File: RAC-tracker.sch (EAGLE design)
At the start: 27 parts, among them J1 U.FL, J2 U.FL, U1 NRF9160-SICA-R, U2 SIM-ST-MFF2, U3 MCP73831, U4 SKY65723-81, U5 MIC5365-1.8YC5-TR

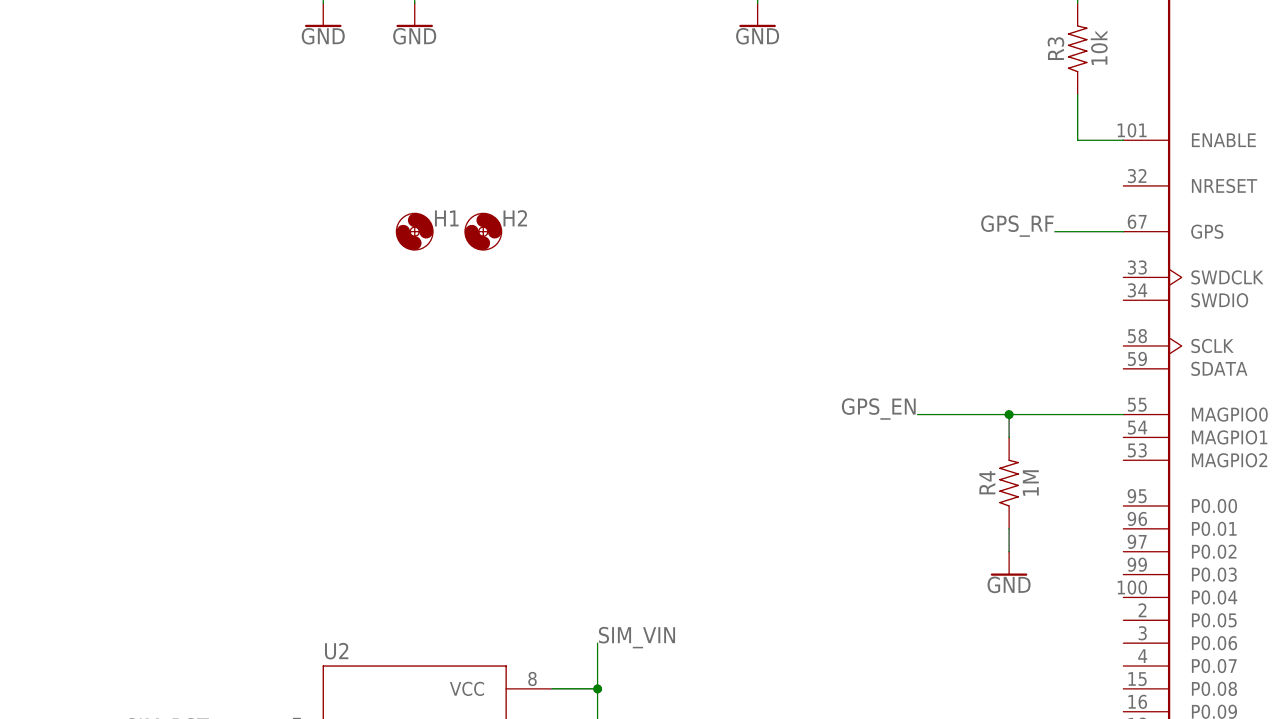
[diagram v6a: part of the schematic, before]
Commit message: Completed routing, cleared DRC errors
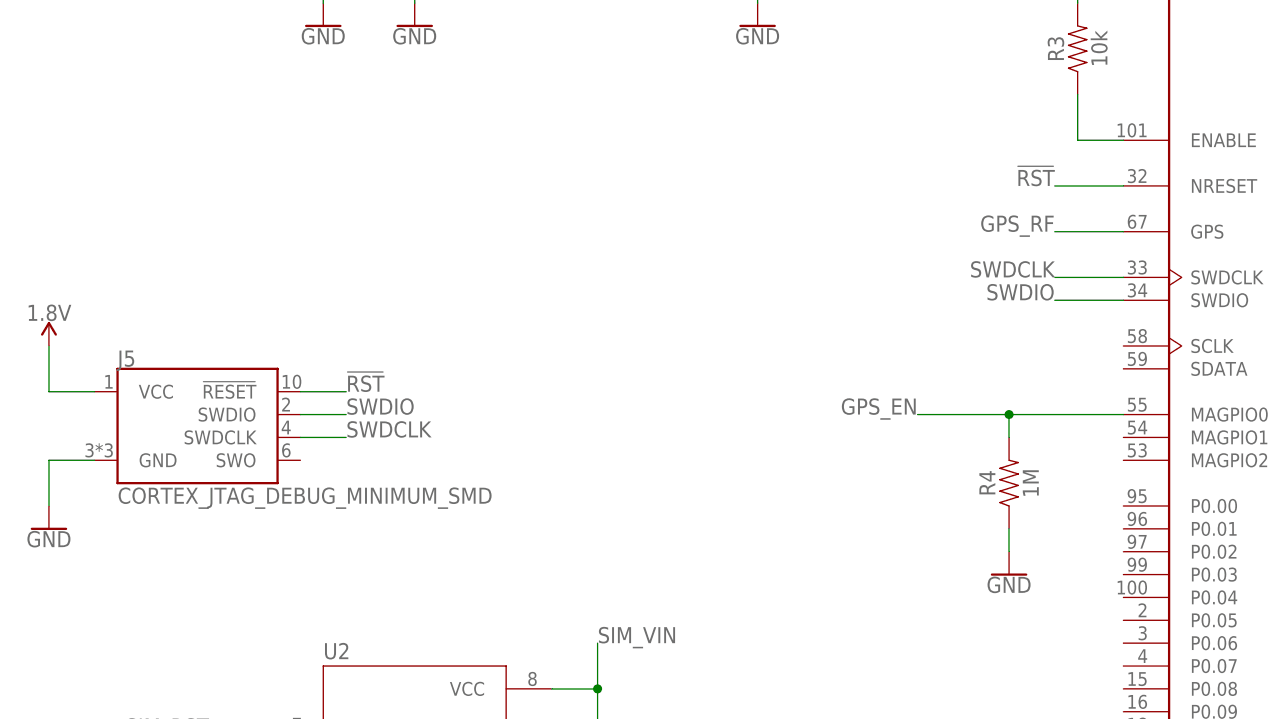
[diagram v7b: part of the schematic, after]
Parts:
- removed H1, H2: MOUNT-HOLE2.8, holes:MOUNT-HOLE2.8
- added J5: CORTEX_JTAG_DEBUG_MINIMUM_SMD, SparkFun-Connectors:CORTEX_JTAG_DEBUG_MINIMUM_SMD
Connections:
- new net !RST: J5.!RESET, U1.NRESET
- new net SWDCLK: J5.SWDCLK, U1.SWDCLK
- new net SWDIO: J5.SWDIO, U1.SWDIO
- net 1.8V: now also J5.VCC
- net GND: now also J5.GND
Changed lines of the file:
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@@
 </classes>
 <parts>
-<part name="H1" library="holes" library_urn="urn:adsk.eagle:library:237" deviceset="MOUNT-HOLE" device="2.8" package3d_urn="urn:adsk.eagle:package:14271/1"/>
-<part name="H2" library="holes" library_urn="urn:adsk.eagle:library:237" deviceset="MOUNT-HOLE" device="2.8" package3d_urn="urn:adsk.eagle:package:14271/1"/>
 <part name="U2" library="rocket-components" deviceset="SIM-ST-MFF2" device=""/>
 <part name="C5" library="SparkFun-Capacitors" library_urn="urn:adsk.eagle:library:510" deviceset="0.1UF" device="-0603-25V-(+80/-20%)" package3d_urn="urn:adsk.eagle:package:37414/1" value="0.1uF"/>
@@
 <part name="SUPPLY16" library="SparkFun-PowerSymbols" library_urn="urn:adsk.eagle:library:530" deviceset="1.8V" device=""/>
 <part name="GND18" library="SparkFun-PowerSymbols" library_urn="urn:adsk.eagle:library:530" deviceset="GND" device=""/>
+<part name="J5" library="SparkFun-Connectors" deviceset="CORTEX_JTAG_DEBUG_MINIMUM" device="_SMD"/>
+<part name="SUPPLY2" library="SparkFun-PowerSymbols" library_urn="urn:adsk.eagle:library:530" deviceset="1.8V" device=""/>
+<part name="GND19" library="SparkFun-PowerSymbols" library_urn="urn:adsk.eagle:library:530" deviceset="GND" device=""/>
 </parts>
 <sheets>
@@
 </plain>
 <instances>
-<instance part="H1" gate="G$1" x="-40.64" y="33.02" smashed="yes">
-<attribute name="NAME" x="-38.608" y="33.6042" size="1.778" layer="95"/>
-</instance>
-<instance part="H2" gate="G$1" x="-33.02" y="33.02" smashed="yes">
-<attribute name="NAME" x="-30.988" y="33.6042" size="1.778" layer="95"/>
-</instance>
 <instance part="U2" gate="G$1" x="-40.64" y="-27.94" smashed="yes">
 <attribute name="NAME" x="-50.8" y="-14.478" size="1.778" layer="95"/>
@@
 <instance part="GND18" gate="1" x="-40.64" y="55.88" smashed="yes">
 <attribute name="VALUE" x="-40.64" y="55.626" size="1.778" layer="96" align="top-center"/>
+</instance>
+<instance part="J5" gate="G$1" x="-63.5" y="10.16" smashed="yes">
+<attribute name="NAME" x="-73.66" y="18.034" size="1.778" layer="95" font="vector"/>
+<attribute name="VALUE" x="-73.66" y="2.794" size="1.778" layer="96" font="vector"/>
+</instance>
+<instance part="SUPPLY2" gate="G$1" x="-81.28" y="20.32" smashed="yes">
+<attribute name="VALUE" x="-81.28" y="23.114" size="1.778" layer="96" align="bottom-center"/>
+</instance>
+<instance part="GND19" gate="1" x="-81.28" y="0" smashed="yes">
+<attribute name="VALUE" x="-81.28" y="-0.254" size="1.778" layer="96" align="top-center"/>
 </instance>
 </instances>
@@
 <wire x1="-40.64" y1="73.66" x2="-35.56" y2="73.66" width="0.1524" layer="91"/>
 </segment>
+<segment>
+<pinref part="GND19" gate="1" pin="GND"/>
+<wire x1="-81.28" y1="2.54" x2="-81.28" y2="7.62" width="0.1524" layer="91"/>
+<pinref part="J5" gate="G$1" pin="GND"/>
+<wire x1="-81.28" y1="7.62" x2="-76.2" y2="7.62" width="0.1524" layer="91"/>
+</segment>
 </net>
 <net name="SIM_VIN" class="0">
@@
 <pinref part="SUPPLY16" gate="G$1" pin="1.8V"/>
 </segment>
-</net>
+<segment>
+<pinref part="J5" gate="G$1" pin="VCC"/>
+<wire x1="-76.2" y1="15.24" x2="-81.28" y2="15.24" width="0.1524" layer="91"/>
+<pinref part="SUPPLY2" gate="G$1" pin="1.8V"/>
+<wire x1="-81.28" y1="15.24" x2="-81.28" y2="20.32" width="0.1524" layer="91"/>
+</segment>
+</net>
+<net name="!RST" class="0">
+<segment>
+<pinref part="U1" gate="G$1" pin="NRESET"/>
+<wire x1="38.1" y1="38.1" x2="30.48" y2="38.1" width="0.1524" layer="91"/>
+<label x="30.48" y="38.1" size="1.778" layer="95" rot="MR0"/>
+</segment>
+<segment>
+<pinref part="J5" gate="G$1" pin="!RESET"/>
+<wire x1="-53.34" y1="15.24" x2="-48.26" y2="15.24" width="0.1524" layer="91"/>
+<label x="-48.26" y="15.24" size="1.778" layer="95"/>
+</segment>
+</net>
+<net name="SWDCLK" class="0">
+<segment>
+<pinref part="U1" gate="G$1" pin="SWDCLK"/>
+<wire x1="38.1" y1="27.94" x2="30.48" y2="27.94" width="0.1524" layer="91"/>
+<label x="30.48" y="27.94" size="1.778" layer="95" rot="MR0"/>
+</segment>
+<segment>
+<pinref part="J5" gate="G$1" pin="SWDCLK"/>
+<wire x1="-53.34" y1="10.16" x2="-48.26" y2="10.16" width="0.1524" layer="91"/>
+<label x="-48.26" y="10.16" size="1.778" layer="95"/>
+</segment>
+</net>
+<net name="SWDIO" class="0">
+<segment>
+<pinref part="U1" gate="G$1" pin="SWDIO"/>
+<wire x1="38.1" y1="25.4" x2="30.48" y2="25.4" width="0.1524" layer="91"/>
+<label x="30.48" y="25.4" size="1.778" layer="95" rot="MR0"/>
+</segment>
+<segment>
+<pinref part="J5" gate="G$1" pin="SWDIO"/>
+<wire x1="-53.34" y1="12.7" x2="-48.26" y2="12.7" width="0.1524" layer="91"/>
+<label x="-48.26" y="12.7" size="1.778" layer="95"/>
+</segment>
+</net>

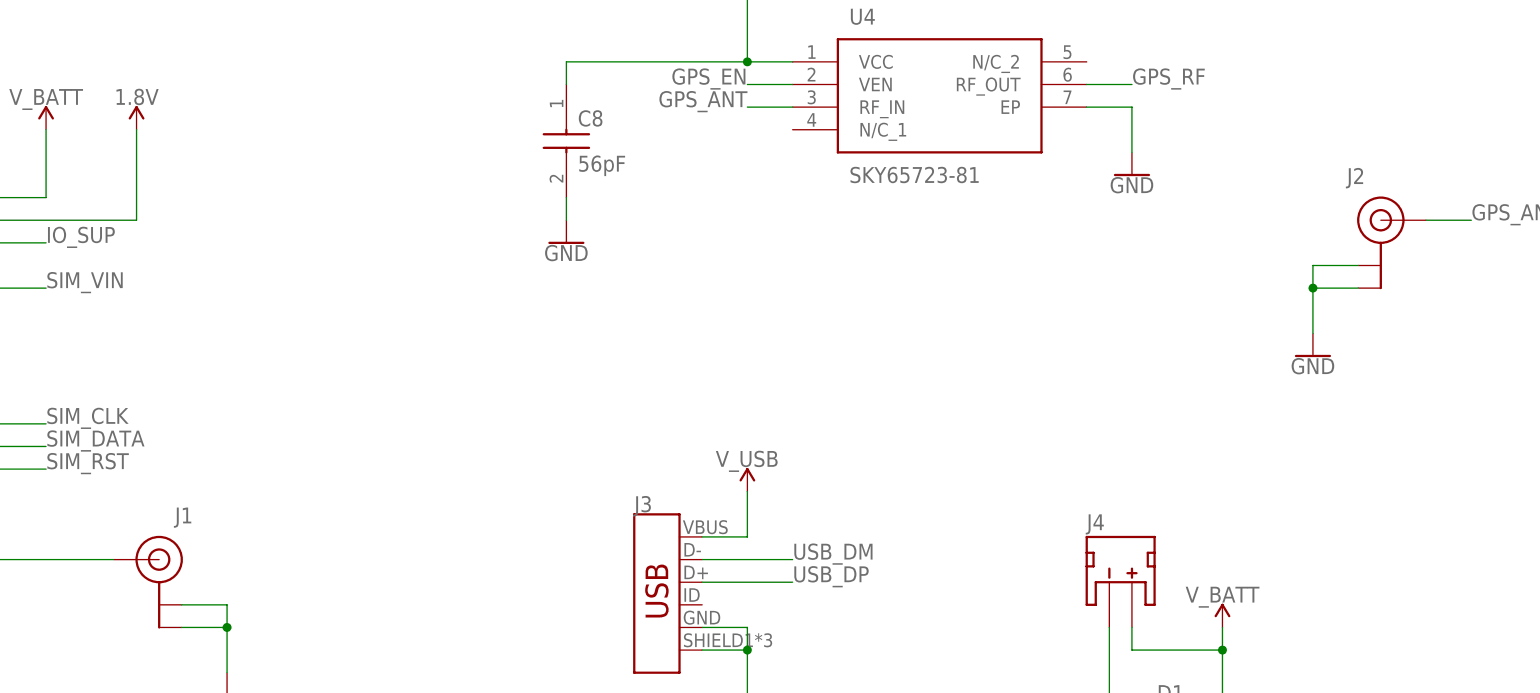
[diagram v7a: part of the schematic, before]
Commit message: Stitched vias in the top ground plane. Ready for fabrication!
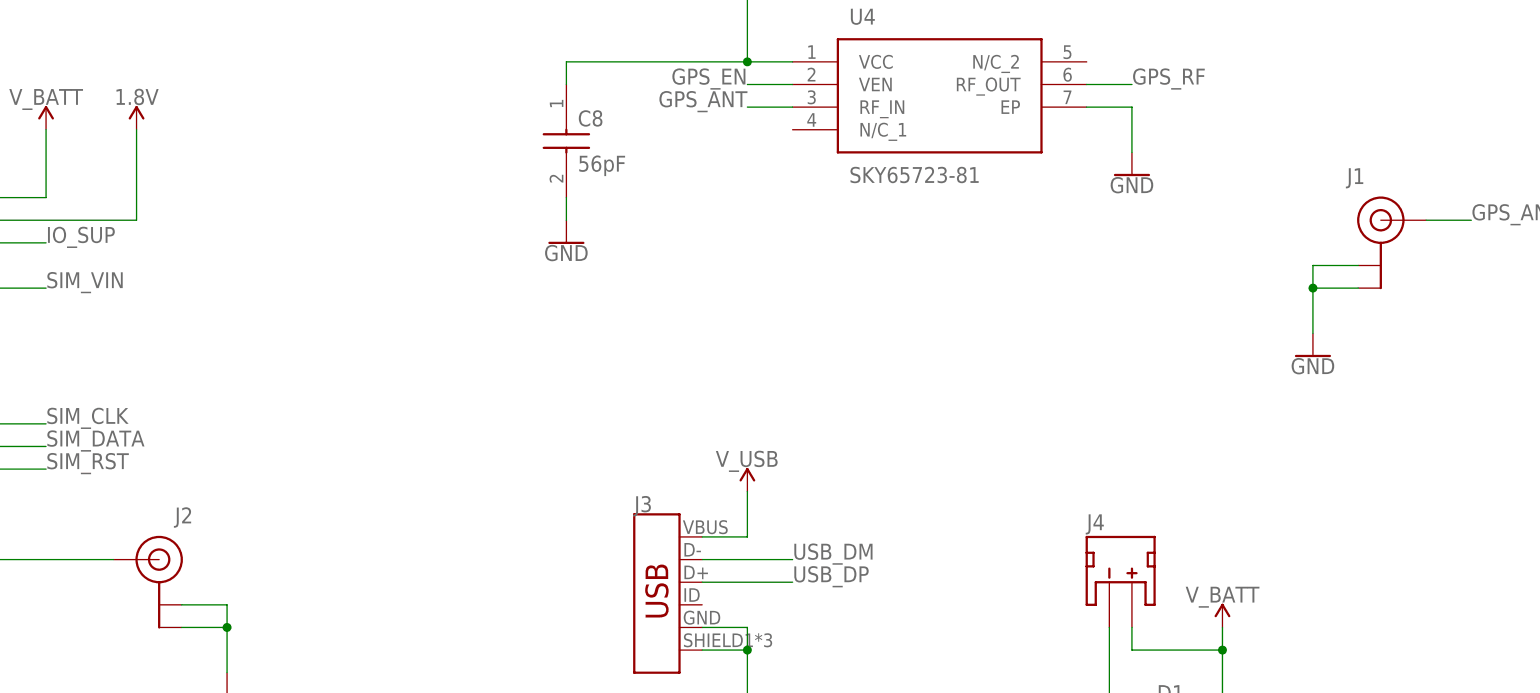
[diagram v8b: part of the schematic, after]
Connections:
- net GPS_ANT: now also J1.SIGNAL; no longer J2.SIGNAL
- net LTE_ANT: now also J2.SIGNAL; no longer J1.SIGNAL
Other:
- moved on the sheet: J1, J2
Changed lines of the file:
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@@
 <part name="R3" library="SparkFun-Resistors" library_urn="urn:adsk.eagle:library:532" deviceset="10KOHM" device="-0603-1/10W-1%" package3d_urn="urn:adsk.eagle:package:39650/1" value="10k"/>
 <part name="SUPPLY11" library="SparkFun-PowerSymbols" library_urn="urn:adsk.eagle:library:530" deviceset="V_BATT" device=""/>
+<part name="J2" library="SparkFun-Connectors" deviceset="U.FL" device="" value="U.FL"/>
+<part name="GND16" library="SparkFun-PowerSymbols" library_urn="urn:adsk.eagle:library:530" deviceset="GND" device=""/>
 <part name="J1" library="SparkFun-Connectors" deviceset="U.FL" device="" value="U.FL"/>
-<part name="GND16" library="SparkFun-PowerSymbols" library_urn="urn:adsk.eagle:library:530" deviceset="GND" device=""/>
-<part name="J2" library="SparkFun-Connectors" deviceset="U.FL" device="" value="U.FL"/>
 <part name="GND17" library="SparkFun-PowerSymbols" library_urn="urn:adsk.eagle:library:530" deviceset="GND" device=""/>
 <part name="D1" library="diode" library_urn="urn:adsk.eagle:library:210" deviceset="SMF5.0AT1" device="" package3d_urn="urn:adsk.eagle:package:43458/1"/>
@@
 <attribute name="VALUE" x="33.02" y="66.294" size="1.778" layer="96" align="bottom-center"/>
 </instance>
-<instance part="J1" gate="G$1" x="109.22" y="17.78" smashed="yes" rot="MR0">
+<instance part="J2" gate="G$1" x="109.22" y="17.78" smashed="yes" rot="MR0">
 <attribute name="NAME" x="113.03" y="21.844" size="1.778" layer="95" rot="MR0"/>
 </instance>
@@
 <attribute name="VALUE" x="116.84" y="2.286" size="1.778" layer="96" align="top-center"/>
 </instance>
-<instance part="J2" gate="G$1" x="246.38" y="55.88" smashed="yes">
+<instance part="J1" gate="G$1" x="246.38" y="55.88" smashed="yes">
 <attribute name="NAME" x="242.57" y="59.944" size="1.778" layer="95"/>
 </instance>
@@
 </segment>
 <segment>
-<pinref part="J1" gate="G$1" pin="GND@1"/>
+<pinref part="J2" gate="G$1" pin="GND@1"/>
 <wire x1="111.76" y1="10.16" x2="116.84" y2="10.16" width="0.1524" layer="91"/>
 <pinref part="GND16" gate="1" pin="GND"/>
 <wire x1="116.84" y1="10.16" x2="116.84" y2="5.08" width="0.1524" layer="91"/>
-<pinref part="J1" gate="G$1" pin="GND@0"/>
+<pinref part="J2" gate="G$1" pin="GND@0"/>
 <wire x1="111.76" y1="12.7" x2="116.84" y2="12.7" width="0.1524" layer="91"/>
 <wire x1="116.84" y1="12.7" x2="116.84" y2="10.16" width="0.1524" layer="91"/>
@@
 </segment>
 <segment>
-<pinref part="J2" gate="G$1" pin="GND@1"/>
+<pinref part="J1" gate="G$1" pin="GND@1"/>
 <wire x1="243.84" y1="48.26" x2="238.76" y2="48.26" width="0.1524" layer="91"/>
 <pinref part="GND17" gate="1" pin="GND"/>
 <wire x1="238.76" y1="48.26" x2="238.76" y2="43.18" width="0.1524" layer="91"/>
-<pinref part="J2" gate="G$1" pin="GND@0"/>
+<pinref part="J1" gate="G$1" pin="GND@0"/>
 <wire x1="243.84" y1="50.8" x2="238.76" y2="50.8" width="0.1524" layer="91"/>
 <wire x1="238.76" y1="50.8" x2="238.76" y2="48.26" width="0.1524" layer="91"/>
@@
 <segment>
 <pinref part="U1" gate="G$1" pin="ANT"/>
-<pinref part="J1" gate="G$1" pin="SIGNAL"/>
+<pinref part="J2" gate="G$1" pin="SIGNAL"/>
 <wire x1="88.9" y1="17.78" x2="104.14" y2="17.78" width="0.1524" layer="91"/>
 </segment>
@@
 <net name="GPS_ANT" class="0">
 <segment>
-<pinref part="J2" gate="G$1" pin="SIGNAL"/>
+<pinref part="J1" gate="G$1" pin="SIGNAL"/>
 <wire x1="251.46" y1="55.88" x2="256.54" y2="55.88" width="0.1524" layer="91"/>
 <label x="256.54" y="55.88" size="1.778" layer="95"/>
